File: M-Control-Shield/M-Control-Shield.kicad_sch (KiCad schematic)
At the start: 4 parts, among them J1 Conn_01x08, J2 Conn_01x06, J3 Conn_01x10, J4 Conn_01x08

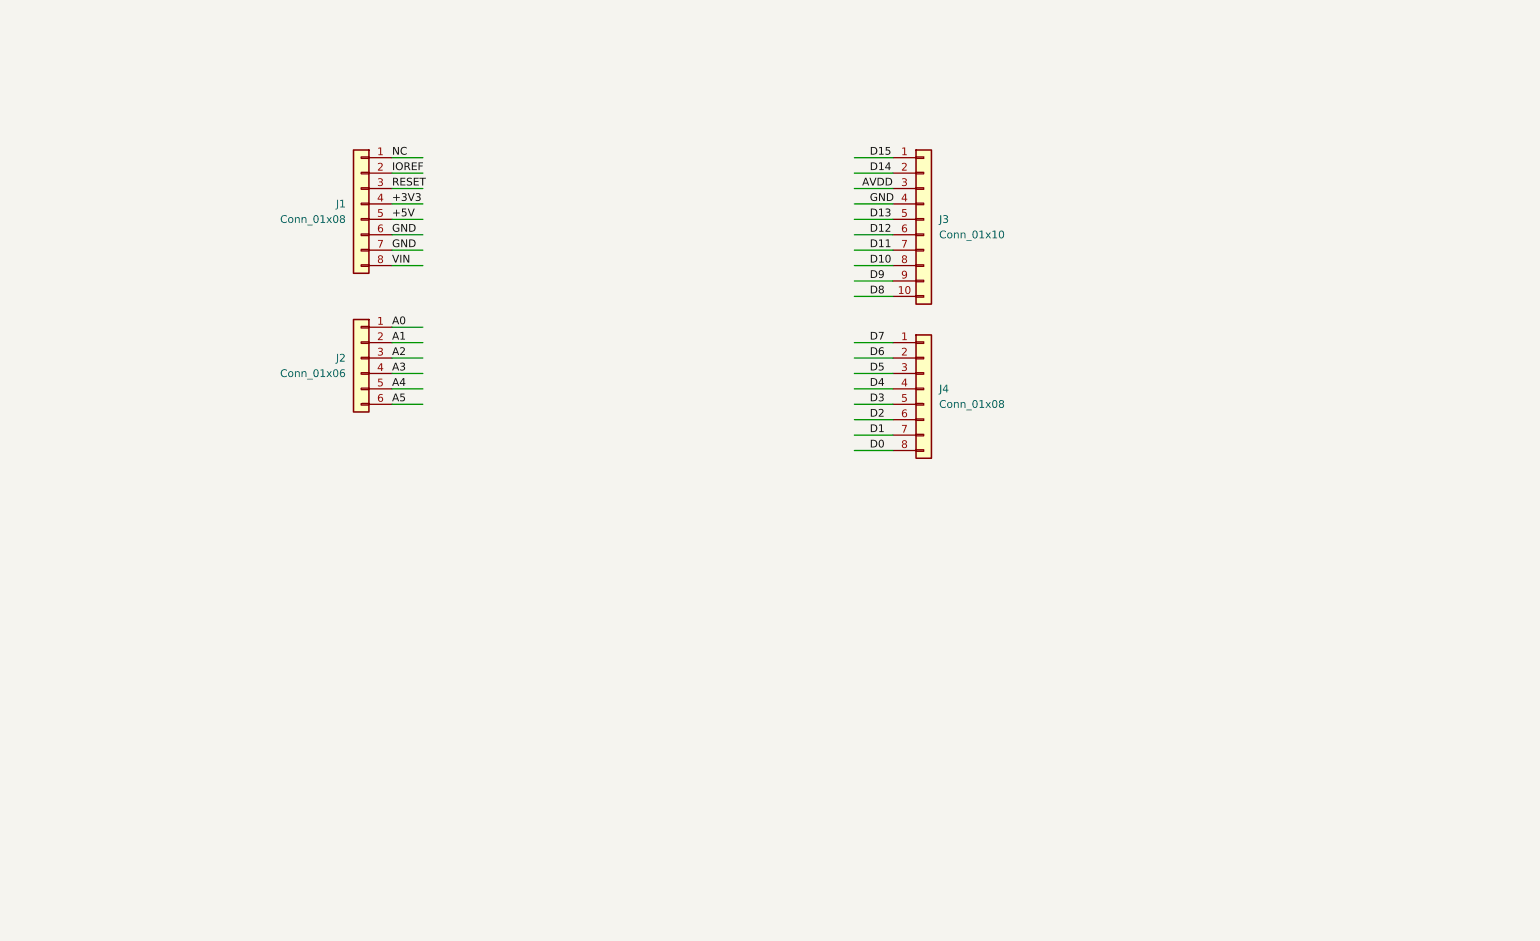
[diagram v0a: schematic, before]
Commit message: Added full bridge and low side current measurement amplifier
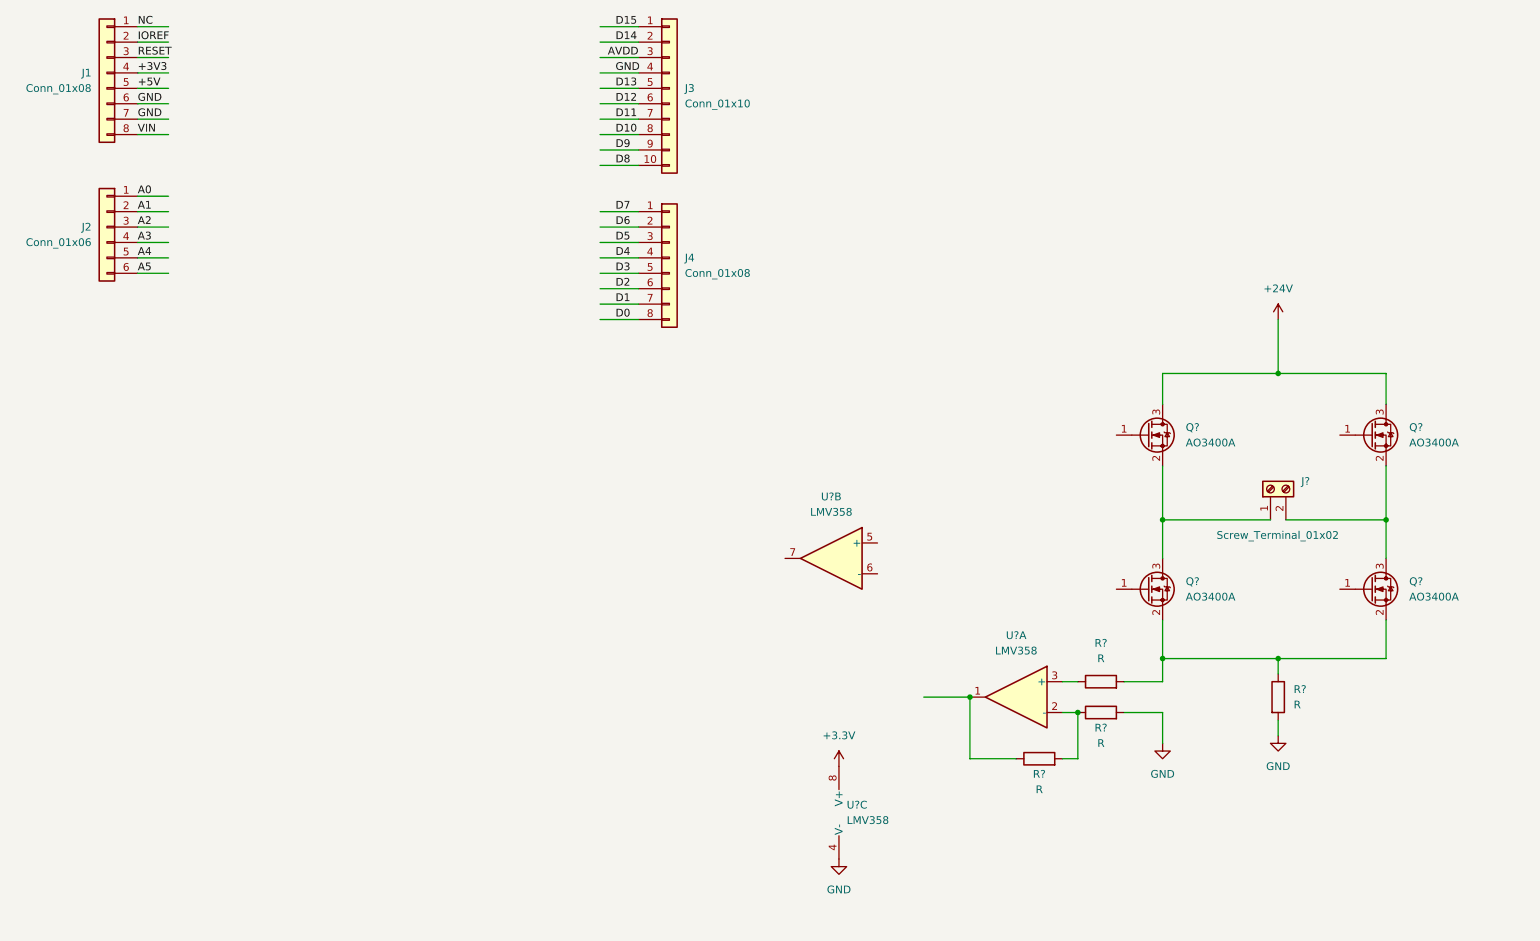
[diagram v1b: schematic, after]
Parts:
- added J?: Screw_Terminal_01x02, symbol Connector:Screw_Terminal_01x02
- added Q? (x4): AO3400A, Package_TO_SOT_SMD:SOT-23, symbol Transistor_FET:AO3400A
- added R? (x4): R, Resistor_SMD:R_0805_2012Metric, symbol Device:R
- added U? (x3): LMV358, symbol Amplifier_Operational:LMV358
- J1: footprint (none) -> Connector_PinHeader_2.54mm:PinHeader_1x08_P2.54mm_Vertical
- J2: footprint (none) -> Connector_PinHeader_2.54mm:PinHeader_1x06_P2.54mm_Vertical
- J3: footprint (none) -> Connector_PinHeader_2.54mm:PinHeader_1x10_P2.54mm_Vertical
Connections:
- net GND: now also R?.2, R?.2, U?.4 (V-)
- new net: Q?.2 (S), Q?.2 (S), R?.1, R?.2
- new net: J?.1 (Pin_1), Q?.2 (S), Q?.3 (D)
- new net: J?.2 (Pin_2), Q?.2 (S), Q?.3 (D)
- new net: R?.1, U?.1
- new net: R?.1, R?.2, U?.2 (-)
- new net: R?.1, U?.3 (+)
- new net +24V: Q?.3 (D), Q?.3 (D)
- new net +3.3V: U?.8 (V+)
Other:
- moved on the sheet: J1, J2, J3, J4

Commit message: Changed HS FETs to PMOS
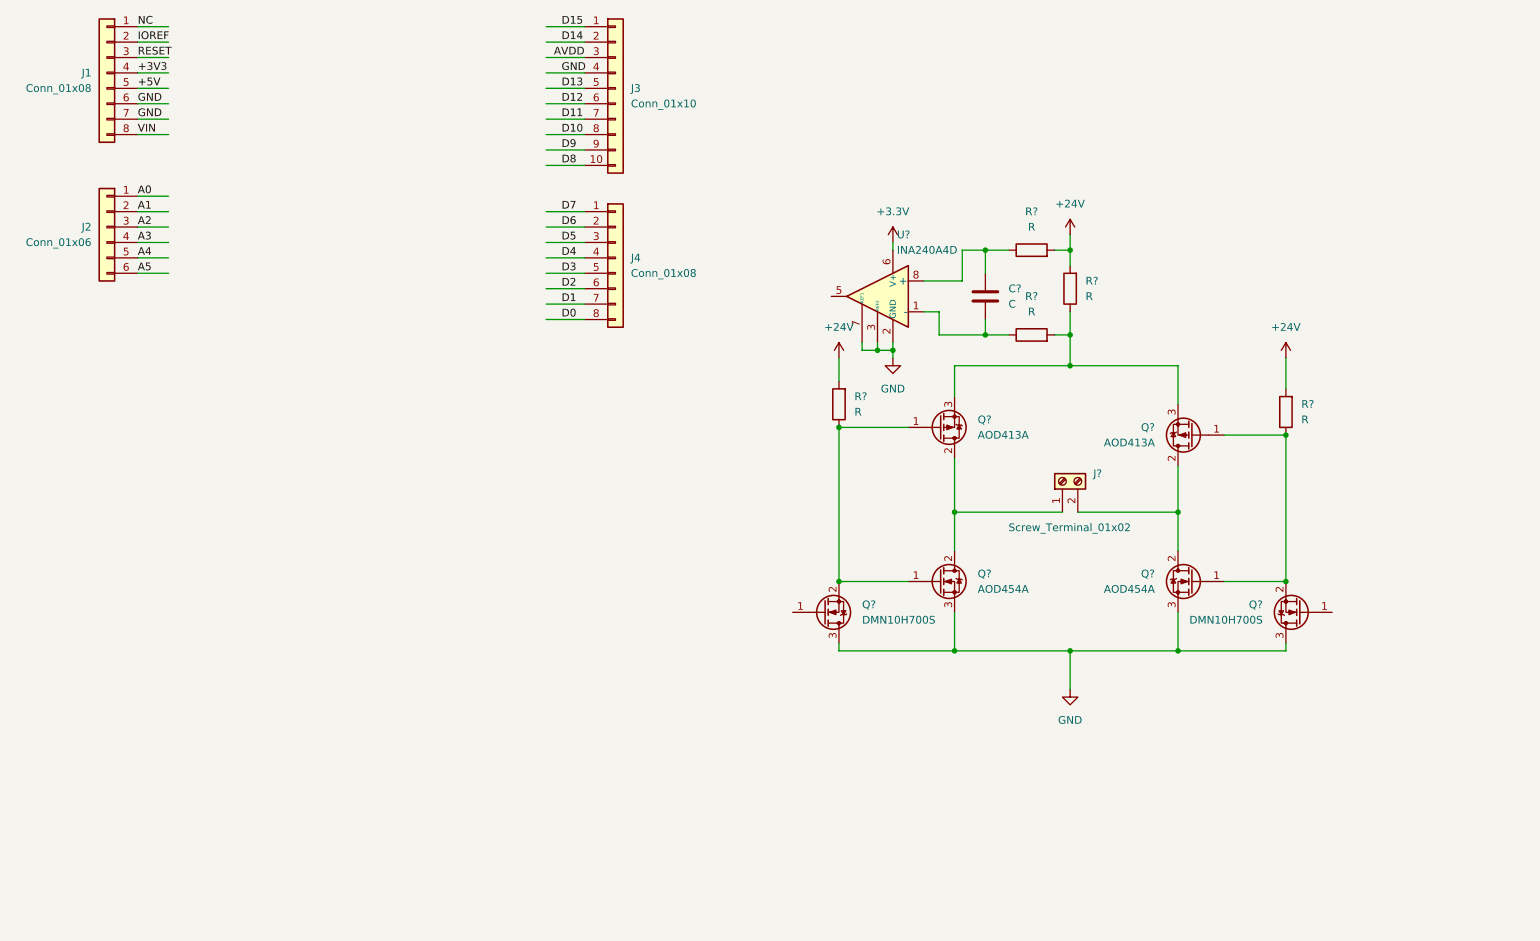
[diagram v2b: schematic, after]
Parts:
- removed Q? (x4): AO3400A, Package_TO_SOT_SMD:SOT-23, symbol Transistor_FET:AO3400A
- removed R? (x4): R, Resistor_SMD:R_0805_2012Metric, symbol Device:R
- removed U? (x3): LMV358, symbol Amplifier_Operational:LMV358
- added C?: C, symbol Device:C
- added Q? (x2): DMN10H700S, Package_TO_SOT_SMD:SOT-23, symbol Transistor_FET:DMN10H700S
- added Q? (x2): AOD454A, Package_TO_SOT_SMD:TO-252-2, symbol Transistor_FET:STD7NK40Z
- added Q? (x2): AOD413A, Package_TO_SOT_SMD:TO-252-2, symbol Transistor_FET:SUD50P04-08
- added R? (x5): R, Resistor_SMD:R_0805_2012Metric, symbol Device:R
- added U?: INA240A4D, Package_SO:SOIC-8_3.9x4.9mm_P1.27mm, symbol Amplifier_Current:INA240A4D
- J?: footprint (none) -> TerminalBlock_Phoenix:TerminalBlock_Phoenix_PT-1,5-2-5.0-H_1x02_P5.00mm_Horizontal
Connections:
- net +24V: now also R?.2, R?.2, R?.2, R?.2
- net +3.3V: now also U?.6 (V+)
- net GND: now also Q?.3 (D), Q?.3 (D), Q?.3 (S), Q?.3 (S), U?.2 (GND), U?.3 (REF2), U?.4 (GND), U?.7 (REF1)
- net at J?.1 (Pin_1): now also Q?.2 (D), Q?.2 (D)
- net at J?.2 (Pin_2): now also Q?.2 (D), Q?.2 (D)
- new net: Q?.1 (G), Q?.1 (G), Q?.2 (S), R?.1 (x2)
- new net: C?.2, R?.1, U?.1 (-)
- new net: C?.1, R?.1, U?.8 (+)
- new net: Q?.3 (S), Q?.3 (S), R?.1, R?.2
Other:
- moved on the sheet: J3, J4, J?

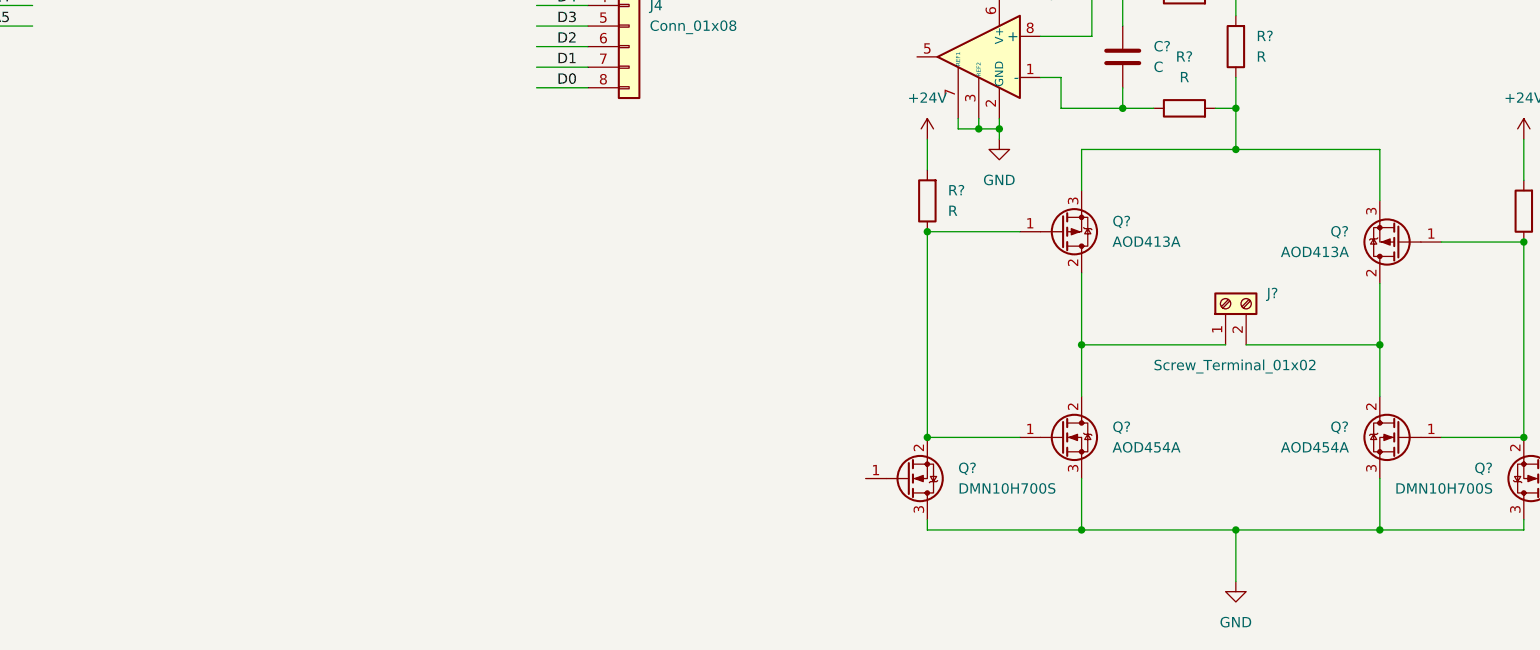
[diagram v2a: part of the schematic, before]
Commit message: Added flyback diodes
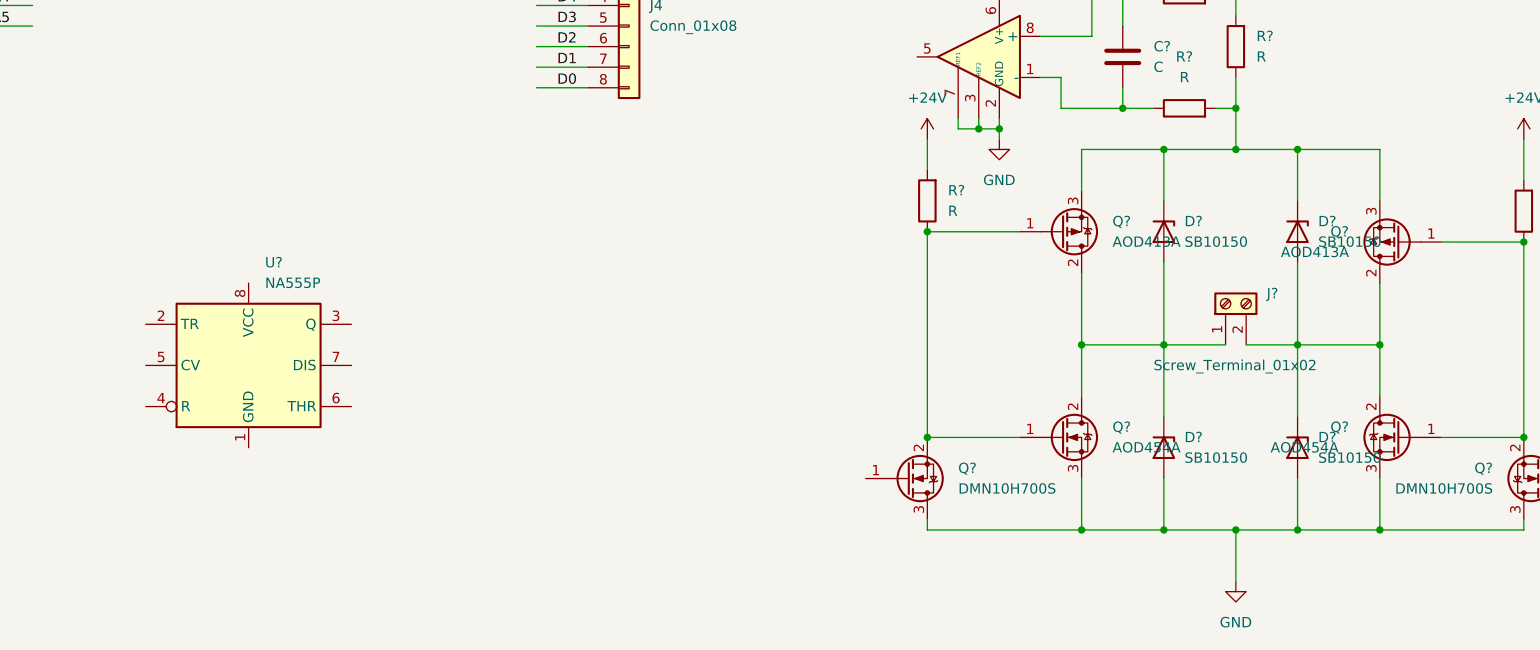
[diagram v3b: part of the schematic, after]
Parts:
- added D? (x4): SB10150, Diode_THT:D_DO-201AD_P12.70mm_Horizontal, symbol Diode:1N53xxB
- added U?: NA555P, Package_DIP:DIP-8_W7.62mm, symbol Timer:NA555P
- C?: footprint (none) -> Capacitor_SMD:C_0603_1608Metric
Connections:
- net GND: now also D?.2 (A), D?.2 (A)
- net at J?.1 (Pin_1), Q?.2 (D), Q?.2 (D): now also D?.1 (K), D?.2 (A)
- net at J?.2 (Pin_2), Q?.2 (D), Q?.2 (D): now also D?.1 (K), D?.2 (A)
- net at Q?.3 (S), Q?.3 (S), R?.1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: now also D?.1 (K), D?.1 (K)

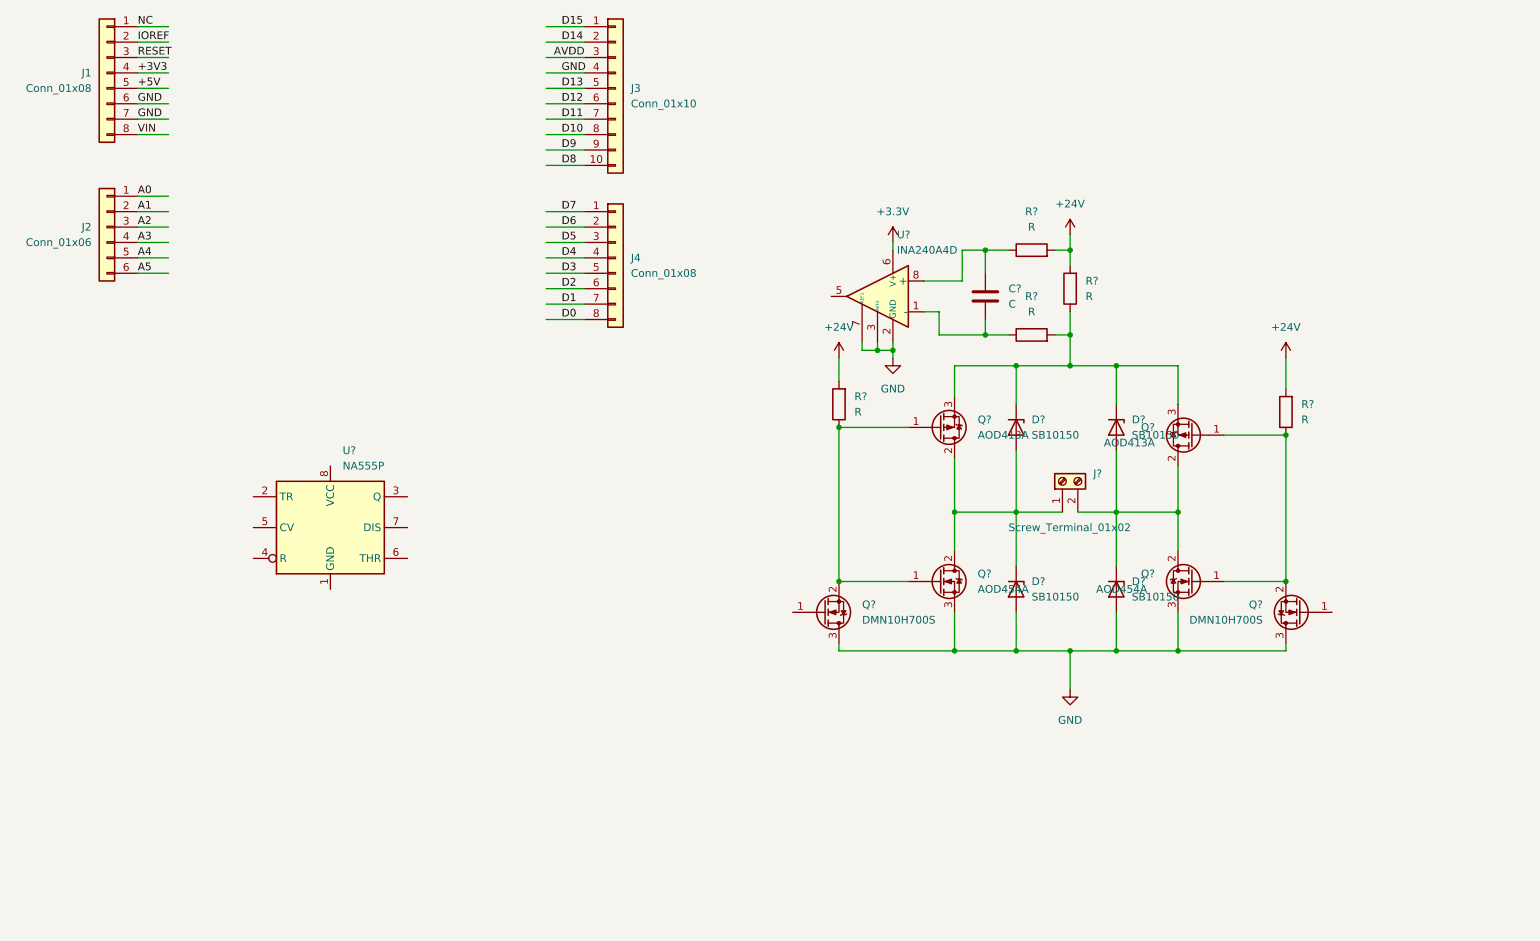
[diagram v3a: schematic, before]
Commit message: Removed gate drives and 555
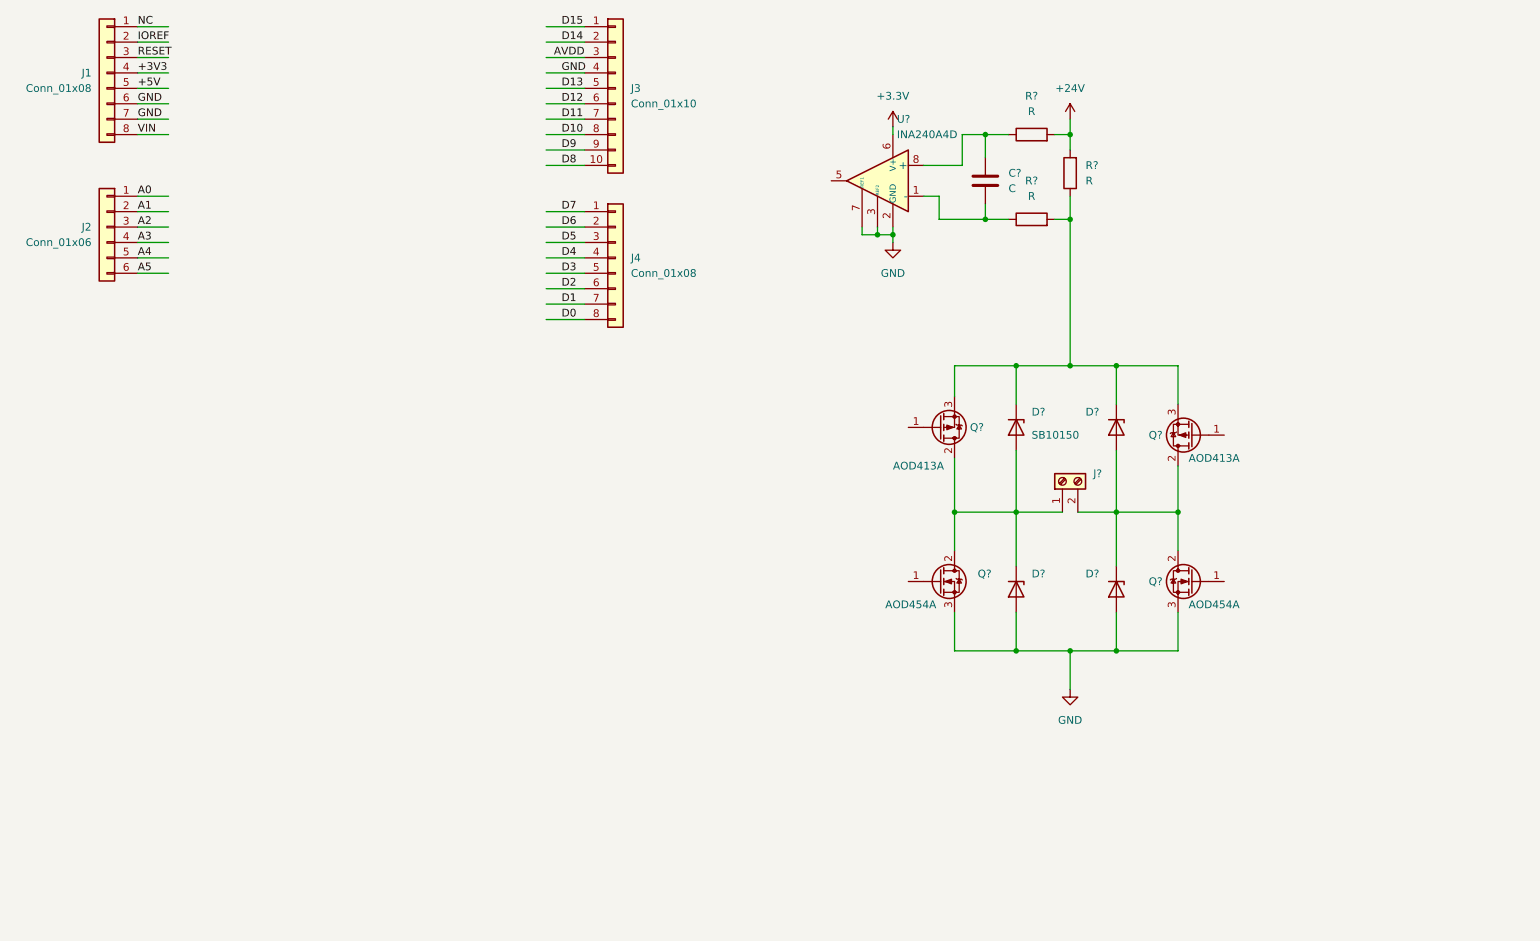
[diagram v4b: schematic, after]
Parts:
- removed Q? (x2): DMN10H700S, Package_TO_SOT_SMD:SOT-23, symbol Transistor_FET:DMN10H700S
- removed R? (x2): R, Resistor_SMD:R_0805_2012Metric, symbol Device:R
- removed U?: NA555P, Package_DIP:DIP-8_W7.62mm, symbol Timer:NA555P
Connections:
- net at Q?.1 (G): no longer Q?.1 (G) (x2)
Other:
- moved on the sheet: C?, R?, U?
